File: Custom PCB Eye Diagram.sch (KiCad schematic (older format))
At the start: 45 parts, among them IC1 DSC1123CI2-125.0000, J1 47272-0001, J10 0878321420, J11 PJ-102B, J12 Conn_01x02, J13 Conn_01x02, J14 Conn_01x01, J15 Conn_01x01, J16 Conn_01x04, J17 Conn_01x04, J2 Conn_01x02, J3 LSHM-150-XX.X-XX-DV-A-N, J4 47272-0001, J5 LSHM-150-XX.X-XX-DV-A-N, J6 Conn_01x03, J7 Conn_01x02, J8 Conn_01x02, J9 Conn_01x02, U1 OKI-78SR-3.3_1.5-W36-C

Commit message: Added test LEDs for practicing FPGA programming
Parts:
- added D2, D3, D4: LED, LED_SMD:LED_0603_1608Metric, symbol Device:LED
- added R5, R6, R7: R, Resistor_SMD:R_0402_1005Metric, symbol Device:R
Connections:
- net GND: now also D2.1 (K), D3.1 (K), D4.1 (K)
- net at J3.53: now also R5.1
- net at J3.56: now also R7.2
- net at J3.68: now also R6.2
- new net: D2.2 (A), R5.2
- new net: D4.2 (A), R7.1
- new net: D3.2 (A), R6.1
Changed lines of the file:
@@
 	0    1    1    0
 $EndComp
+$Comp
+L Device:LED D2
+U 1 1 5F16AC94
+P 10250 4800
+F 0 "D2" H 10243 5016 50  0000 C CNN
+F 1 "LED" H 10243 4925 50  0000 C CNN
+F 2 "LED_SMD:LED_0603_1608Metric" H 10250 4800 50  0001 C CNN
+F 3 "~" H 10250 4800 50  0001 C CNN
+	1    10250 4800
+	1    0    0    -1
+$EndComp
+$Comp
+L Device:R R5
+U 1 1 5F17407B
+P 10650 4800
+F 0 "R5" V 10443 4800 50  0000 C CNN
+F 1 "R" V 10534 4800 50  0000 C CNN
+F 2 "Resistor_SMD:R_0402_1005Metric" V 10580 4800 50  0001 C CNN
+F 3 "~" H 10650 4800 50  0001 C CNN
+	1    10650 4800
+	0    1    1    0
+$EndComp
+Wire Wire Line
+	10400 4800 10500 4800
+Wire Wire Line
+	10800 4800 11050 4800
+$Comp
+L power:GND #PWR039
+U 1 1 5F1802B8
+P 10100 4800
+F 0 "#PWR039" H 10100 4550 50  0001 C CNN
+F 1 "GND" V 10105 4672 50  0000 R CNN
+F 2 "" H 10100 4800 50  0001 C CNN
+F 3 "" H 10100 4800 50  0001 C CNN
+	1    10100 4800
+	0    1    1    0
+$EndComp
+$Comp
+L Device:R R7
+U 1 1 5F180FD3
+P 12500 4900
+F 0 "R7" V 12293 4900 50  0000 C CNN
+F 1 "R" V 12384 4900 50  0000 C CNN
+F 2 "Resistor_SMD:R_0402_1005Metric" V 12430 4900 50  0001 C CNN
+F 3 "~" H 12500 4900 50  0001 C CNN
+	1    12500 4900
+	0    1    1    0
+$EndComp
+$Comp
+L Device:LED D4
+U 1 1 5F181D15
+P 12900 4900
+F 0 "D4" H 12893 4645 50  0000 C CNN
+F 1 "LED" H 12893 4736 50  0000 C CNN
+F 2 "LED_SMD:LED_0603_1608Metric" H 12900 4900 50  0001 C CNN
+F 3 "~" H 12900 4900 50  0001 C CNN
+	1    12900 4900
+	-1   0    0    1
+$EndComp
+Wire Wire Line
+	11950 4900 12350 4900
+Wire Wire Line
+	12650 4900 12750 4900
+$Comp
+L power:GND #PWR041
+U 1 1 5F18F286
+P 13050 4900
+F 0 "#PWR041" H 13050 4650 50  0001 C CNN
+F 1 "GND" V 13055 4772 50  0000 R CNN
+F 2 "" H 13050 4900 50  0001 C CNN
+F 3 "" H 13050 4900 50  0001 C CNN
+	1    13050 4900
+	0    -1   -1   0
+$EndComp
+$Comp
+L Device:R R6
+U 1 1 5F1902B3
+P 12350 5500
+F 0 "R6" V 12143 5500 50  0000 C CNN
+F 1 "R" V 12234 5500 50  0000 C CNN
+F 2 "Resistor_SMD:R_0402_1005Metric" V 12280 5500 50  0001 C CNN
+F 3 "~" H 12350 5500 50  0001 C CNN
+	1    12350 5500
+	0    1    1    0
+$EndComp
+Wire Wire Line
+	11950 5500 12200 5500
+$Comp
+L Device:LED D3
+U 1 1 5F196D5C
+P 12800 5500
+F 0 "D3" H 12793 5245 50  0000 C CNN
+F 1 "LED" H 12793 5336 50  0000 C CNN
+F 2 "LED_SMD:LED_0603_1608Metric" H 12800 5500 50  0001 C CNN
+F 3 "~" H 12800 5500 50  0001 C CNN
+	1    12800 5500
+	-1   0    0    1
+$EndComp
+Wire Wire Line
+	12500 5500 12650 5500
+$Comp
+L power:GND #PWR040
+U 1 1 5F1A5F62
+P 12950 5500
+F 0 "#PWR040" H 12950 5250 50  0001 C CNN
+F 1 "GND" V 12955 5372 50  0000 R CNN
+F 2 "" H 12950 5500 50  0001 C CNN
+F 3 "" H 12950 5500 50  0001 C CNN
+	1    12950 5500
+	0    -1   -1   0
+$EndComp
 $EndSCHEMATC

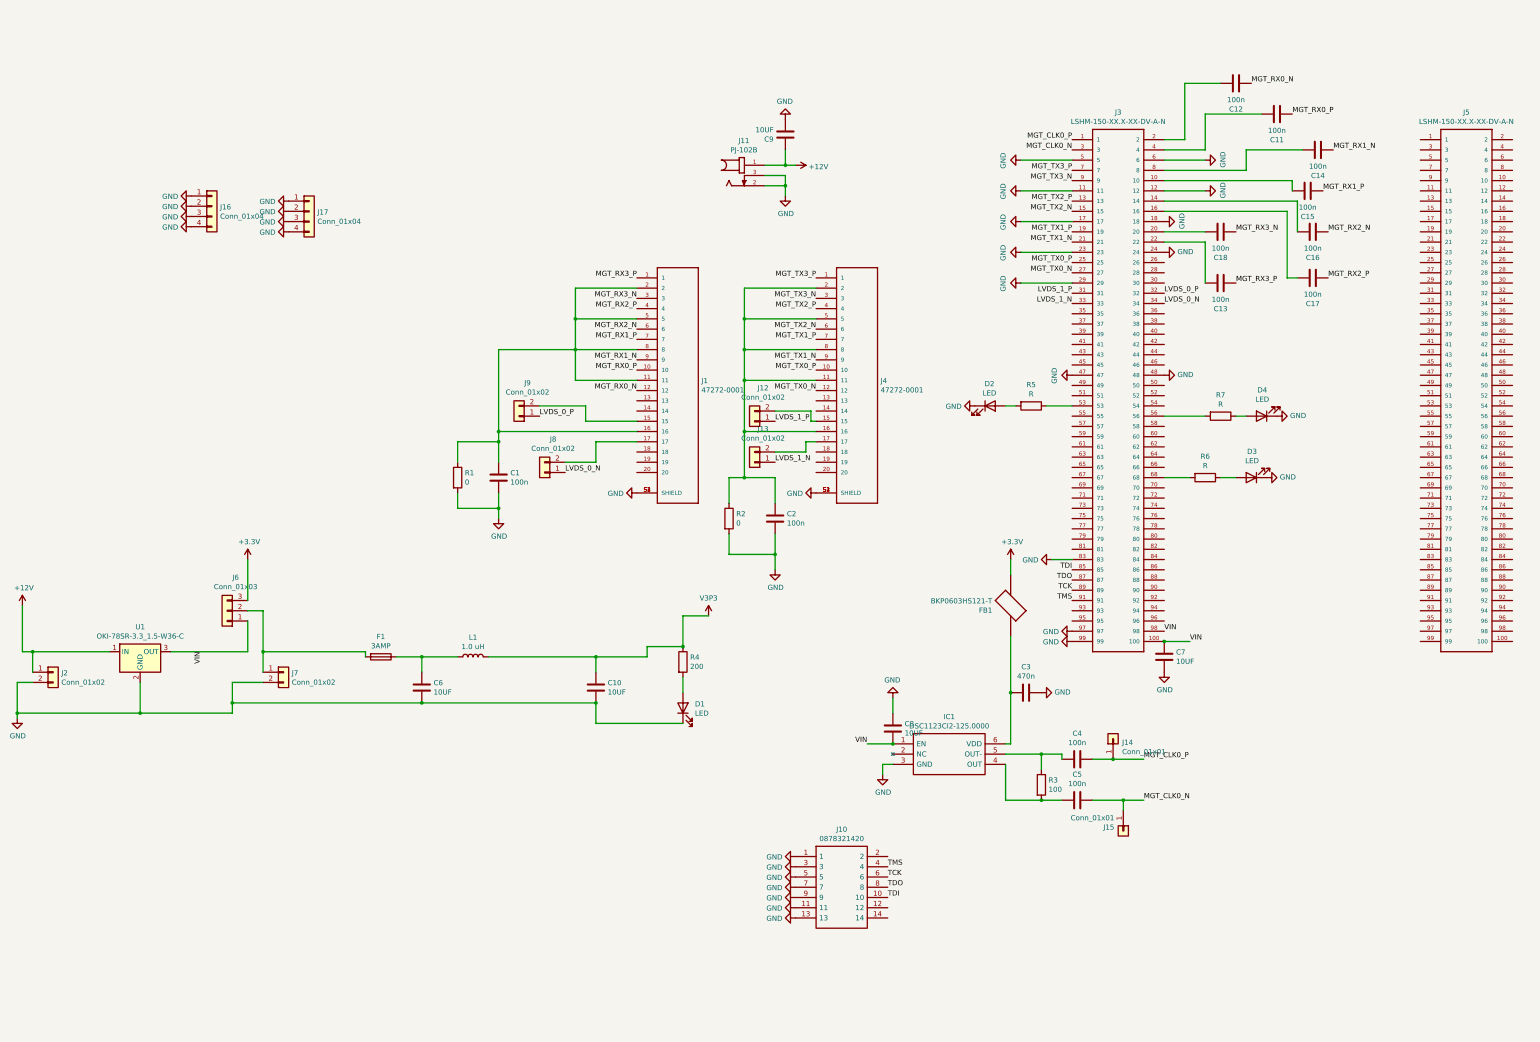
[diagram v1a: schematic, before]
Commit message: Fixed test LED setup for FPGA programming practice
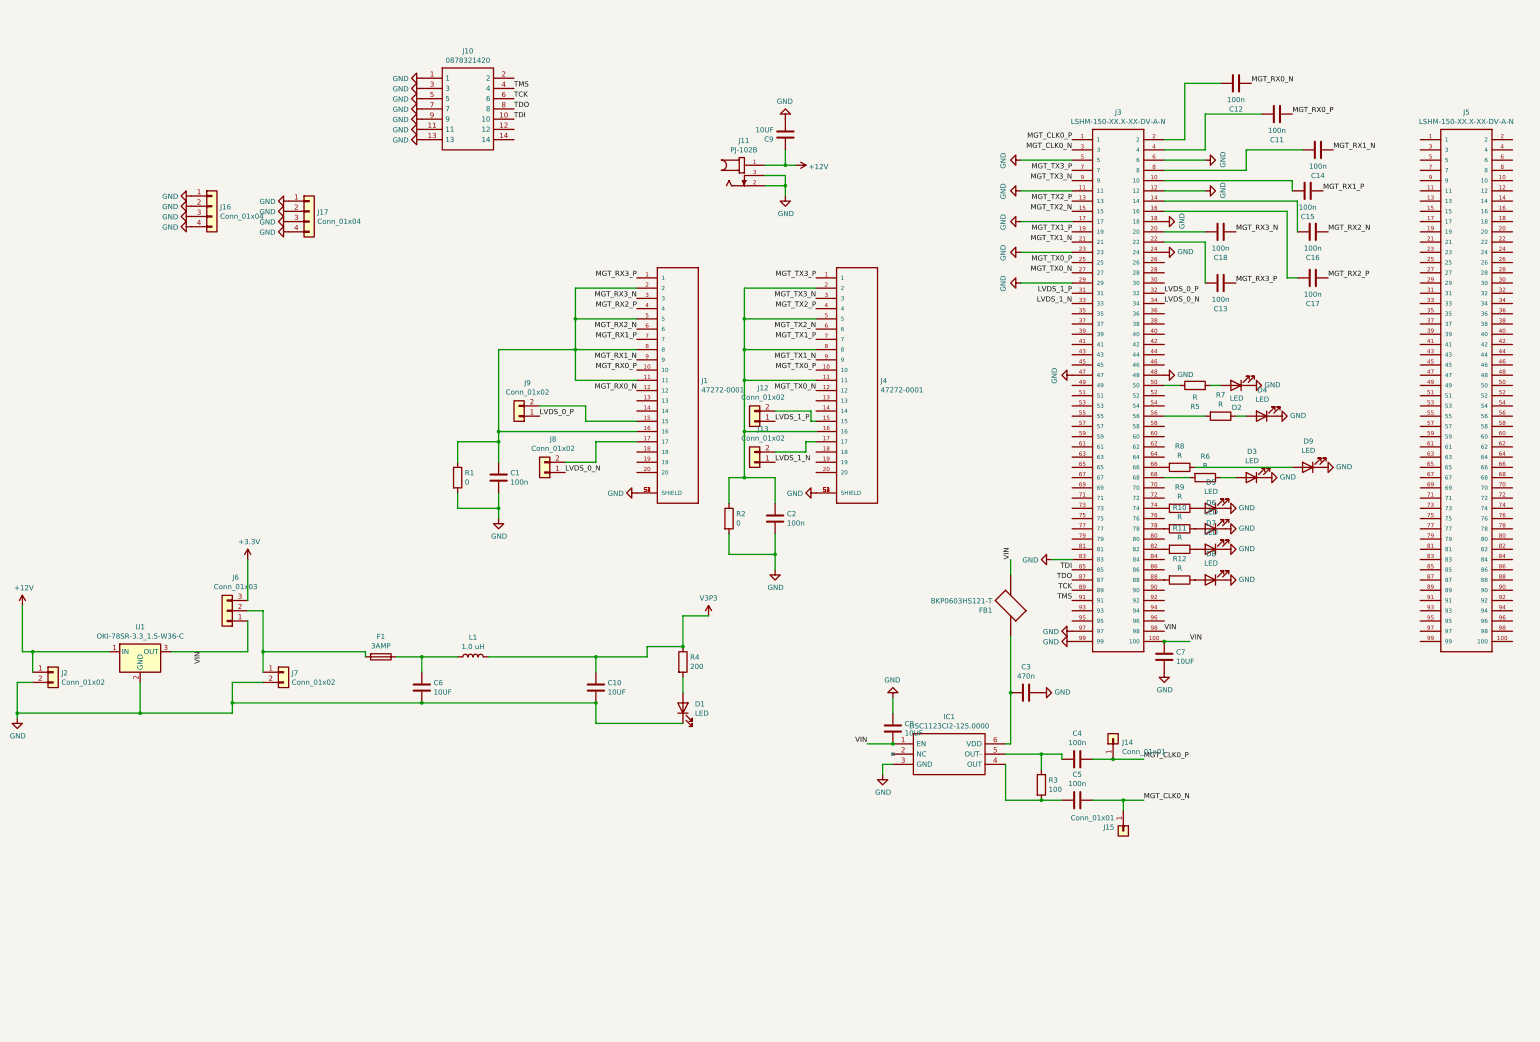
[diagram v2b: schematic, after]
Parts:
- added D5, D6, D7, D8, D9: LED, LED_SMD:LED_0603_1608Metric, symbol Device:LED
- added R10, R11, R12, R8, R9: R, Resistor_SMD:R_0402_1005Metric, symbol Device:R
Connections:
- net +3V3: no longer FB1.2
- net GND: now also D5.1 (K), D6.1 (K), D7.1 (K), D8.1 (K), D9.1 (K)
- net VIN: now also FB1.2
- net at J3.50: now also R5.1
- net at J3.53: no longer R5.1
- net at J3.66: now also R8.2
- net at J3.74: now also R9.2
- net at J3.78: now also R10.2
- net at J3.82: now also R11.2
- net at J3.88: now also R12.2
- new net: D9.2 (A), R8.1
- new net: D5.2 (A), R9.1
- new net: D6.2 (A), R10.1
- new net: D7.2 (A), R11.1
- new net: D8.2 (A), R12.1
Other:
- moved on the sheet: D2, J10, R5

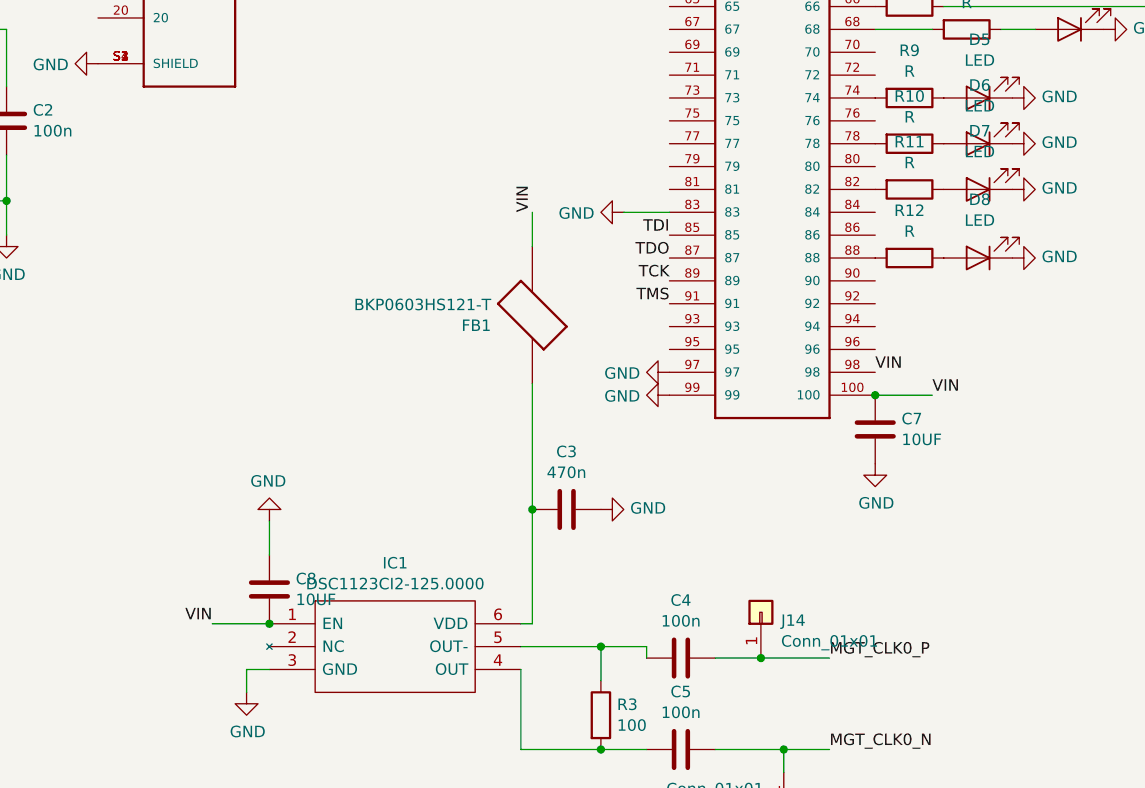
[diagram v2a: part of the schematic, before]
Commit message: Added LBNL logo, name, and changed VIN layer to V3P3 layer
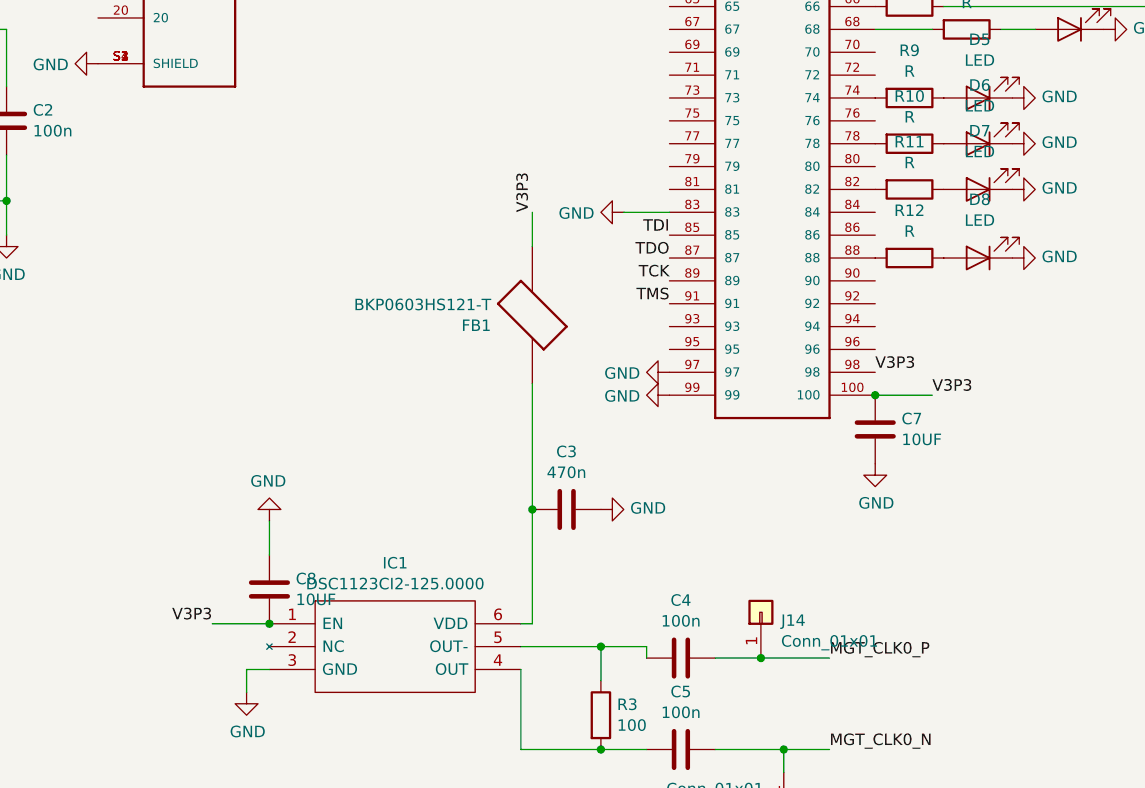
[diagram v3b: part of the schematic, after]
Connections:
- net VIN: no longer C7.1, C8.2, FB1.2, IC1.1 (EN), J3.100, J3.98
- new net V3P3: C7.1, C8.2, FB1.2, IC1.1 (EN), J3.100, J3.98
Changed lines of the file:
@@
 Text Label 2550 7200 3    50   ~ 0
-VIN
-Text Label 11950 7000 0    50   ~ 0
-VIN
-Text Label 12200 7100 0    50   ~ 0
 VIN
 $Comp
@@
 	1    0    0    -1
 $EndComp
-Text Label 9050 8100 2    50   ~ 0
-VIN
 Wire Wire Line
 	9200 8400 9200 8300
@@
 $EndComp
 Text Label 10450 6300 1    50   ~ 0
-VIN
+V3P3
 $Comp
 L power:+3.3V #PWR?
@@
 	1    0    0    -1
 $EndComp
+Text Label 11950 7000 0    50   ~ 0
+V3P3
+Text Label 12200 7100 0    50   ~ 0
+V3P3
+Text Label 9050 8100 2    50   ~ 0
+V3P3
 $EndSCHEMATC

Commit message: Another iteration of the PCB and made some updates to the BOM
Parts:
- removed J14, J15: Conn_01x01, Connector_PinHeader_2.54mm:PinHeader_1x01_P2.54mm_Vertical, symbol Connector_Generic:Conn_01x01
- added J15, J17: Conn_01x02, Connector_PinHeader_2.54mm:PinHeader_1x02_P2.54mm_Vertical, symbol Connector_Generic:Conn_01x02
- R2: renamed from R4; footprint Resistor_SMD:R_0402_1005Metric -> Resistor_SMD:R_0603_1608Metric
- renumbered C6 to C1, C7 to C10, C18 to C11, C13 to C12, C12 to C13, C11 to C14, C14 to C18, C1 to C2, C10 to C3, C2 to C4, C9 to C5, C8 to C6, C3 to C7, C4 to C8, C5 to C9, D5 to D2, D6 to D3, D7 to D4, D8 to D5, D2 to D6, D3 to D7, D4 to D8, J2 to J1, J11 to J10, J12 to J11, J13 to J12, J4 to J13, J3 to J14, J5 to J16, J16 to J2, J6 to J3, J7 to J4, J17 to J5, J10 to J6, J9 to J7, J1 to J9, R5 to R10, R6 to R11, R7 to R12, R2 to R3, R3 to R4, R8 to R5, R9 to R6, R10 to R7, R11 to R8, R12 to R9
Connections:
- net V3P3 is gone; now on net +3V3: C10.1, C6.2, FB1.2, IC1.1 (EN), J14.100, J14.98
- net +3V3: now also C3.1, L1.2, R2.1, J17.1 (Pin_1); no longer J3.3 (Pin_3)
- net GND: now also J17.2 (Pin_2)
- net LVDS_0_N: now also J14.32; no longer J14.34
- net LVDS_0_P: now also J14.34; no longer J14.32
- net MGT_CLK0_N: now also J14.1, J15.2 (Pin_2); no longer J14.3
- net MGT_CLK0_P: now also J14.3, J15.1 (Pin_1); no longer J14.1
- net LVDS_0_J_P: now reaches J7.2 (Pin_2), J9.15
- net LVDS_0_J_N: now reaches J8.2 (Pin_2), J9.17
- net MGT_RX1_C_P: now reaches C15.1, J14.10
- net MGT_RX2_C_N: now reaches C16.1, J14.14
- net MGT_RX2_C_P: now reaches C17.1, J14.16
- net MGT_RX0_C_N: now reaches C13.1, J14.2
- net MGT_RX3_C_N: now reaches C11.2, J14.20
- net MGT_RX3_C_P: now reaches C12.1, J14.22
- net MGT_RX0_C_P: now reaches C14.1, J14.4
- net MGT_RX1_C_N: now reaches C18.1, J14.8
- net MGT_CLK_C_P: now reaches C8.2, IC1.5 (OUT-)
- net MGT_CLK_C_P: now also R4.2; no longer R4.1
- net MGT_CLK_C_N: now reaches C9.2, IC1.4 (OUT)
- net MGT_CLK_C_N: now also R4.1; no longer R4.2
- net LVDS_1_J_P: now reaches J11.2 (Pin_2), J13.15
- net LVDS_1_J_N: now reaches J12.2 (Pin_2), J13.17
- net V3P3RAW: now reaches F1.2, J3.2 (Pin_2), J4.1 (Pin_1)
- net VIN renamed DCV3P3
- new net V3P3EXTERNAL: J3.3 (Pin_3)

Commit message: PCB 2.0
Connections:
- net +3V3: now also J16.97, J16.99; no longer J14.100, J14.98
- net GND: now also J16.100, J16.11, J16.12, J16.17, J16.18, J16.23, J16.24, J16.29, J16.30, J16.47, J16.48, J16.5, J16.6, J16.66, J16.84, J16.98; no longer J14.11, J14.12, J14.17, J14.18, J14.23, J14.24, J14.29, J14.47, J14.48, J14.5, J14.6, J14.83, J14.97, J14.99
- net LVDS_0_N: now also J16.33; no longer J14.32
- net LVDS_0_P: now also J16.31; no longer J14.34
- net LVDS_1_N: now also J16.32; no longer J14.33
- net LVDS_1_P: now also J16.34; no longer J14.31
- net MGT_CLK0_N: now also J16.4; no longer J14.1
- net MGT_CLK0_P: now also J16.2; no longer J14.3
- net MGT_RX0_C_N: now also J16.21; no longer J14.2
- net MGT_RX0_C_P: now also J16.19; no longer J14.4
- net MGT_RX1_C_N: now also J16.15; no longer J14.8
- net MGT_RX1_C_P: now also J16.13; no longer J14.10
- net MGT_RX2_C_N: now also J16.9; no longer J14.14
- net MGT_RX2_C_P: now also J16.7; no longer J14.16
- net MGT_RX3_C_N: now also J16.3; no longer J14.20
- net MGT_RX3_C_P: now also J16.1; no longer J14.22
- net MGT_TX0_N: now also J16.8; no longer J14.27
- net MGT_TX0_P: now also J16.10; no longer J14.25
- net MGT_TX1_N: now also J16.14; no longer J14.21
- net MGT_TX1_P: now also J16.16; no longer J14.19
- net MGT_TX2_N: now also J16.20; no longer J14.15
- net MGT_TX2_P: now also J16.22; no longer J14.13
- net MGT_TX3_N: now also J16.26; no longer J14.9
- net MGT_TX3_P: now also J16.28; no longer J14.7
- net TCK: now also J16.90; no longer J14.89
- net TDI: now also J16.86; no longer J14.85
- net TDO: now also J16.88; no longer J14.87
- net TMS: now also J16.92; no longer J14.91
- net at J14.50: no longer R10.1
- net at J14.56: no longer R12.2
- net at J14.66: no longer R5.2
- net at J14.68: no longer R11.2
- net at J14.74: no longer R6.2
- net at J14.78: no longer R7.2
- net at J14.82: no longer R8.2
- net at J14.88: no longer R9.2
- net at J16.49: now also R9.2
- net at J16.55: now also R8.2
- net at J16.65: now also R7.2
- net at J16.67: now also R6.2
- net at J16.73: now also R11.2
- net at J16.77: now also R5.2
- net at J16.81: now also R12.2
- net at J16.87: now also R10.1
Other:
- moved on the sheet: C10, C11, C12, C13, C14, C15, C16, C17, C18, C6, C7, C8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
